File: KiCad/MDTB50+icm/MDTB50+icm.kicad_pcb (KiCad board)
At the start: 4 copper layers, 14.7 x 31.5 mm, 37 parts, among them SW1 1TS026A-1100-0550-CT, U1 ICM-45686, U2 TXS0102DQER, U4 SSP7615-18DFR, U5 SSP7615-33DFR

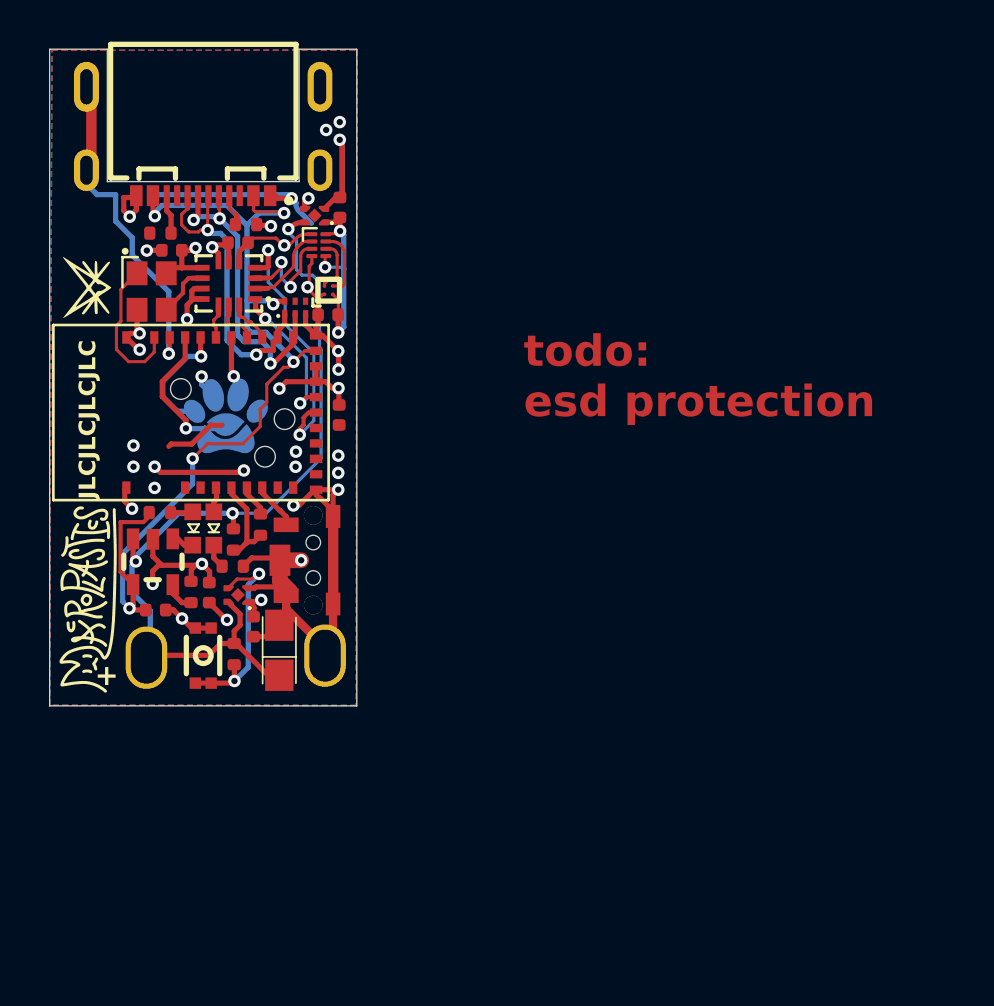
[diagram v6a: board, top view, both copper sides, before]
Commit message: - Added 0201 version with: DCDC, RGB LED, replaced charger IC, shortened   by 2mm.
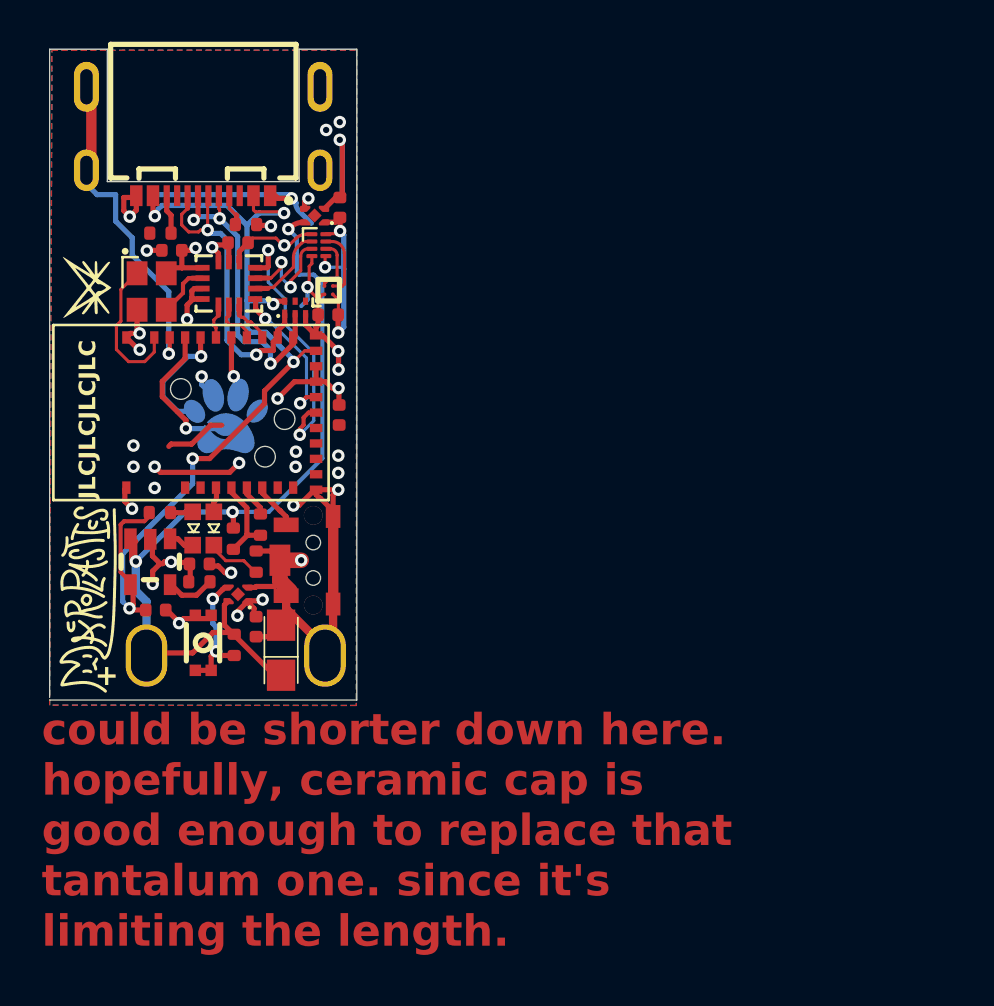
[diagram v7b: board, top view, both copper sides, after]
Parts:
- D1: value TPD3E001DRYR -> TPD3E001DRYR-TP
- ETA4054S1F1: value ~ -> ETA4054S1F1
- S1: value ~ -> GT-TC020B-H035-L05
- U3: value ~ -> QMC6309
- X1: value ~ -> SX2M32.768KM20F30TNN
- moved C1n1 1.47 mm to (116.2, 88.1), turned to 180 degrees
- moved R1n1 1.15 mm to (118.9, 87.9), turned to -90 degrees
- moved R1C1 0.64 mm to (116.1, 88.9), turned to 180 degrees
- moved SW1 0.61 mm to (116.3, 91.8)
- moved R1C2 0.44 mm to (117.8, 91.9)
- moved ETA4054S1F1 0.13 mm to (113.8, 88.0)
- moved C2R1 0.12 mm to (118.9, 91.1)
- moved B+1 0.10 mm to (113.6, 92.5)
- moved C1 0.08 mm to (120.1, 92.2)
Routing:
- net Net-(U4-EN): track 10.2 -> 6.45 mm
- net +1.8V: track 36.7 -> 38.5 mm, vias 8 -> 9
- net Net-(LED1n1-K): track 1.18 -> 2.61 mm
- net GND: track 98.7 -> 97.6 mm
- net Net-(ETA4054S1F1-ISET): track 1.48 -> 2.30 mm
- net VBUS: track 45.5 -> 44.8 mm
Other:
- board size 14.7 x 31.5 mm -> 14.7 x 31.2 mm
- board text added: "could be shorter down here. hopefully, ceramic cap is good enough to replace that tantalum one. since it's limiting the length."
- board text removed: "todo: esd protection"
